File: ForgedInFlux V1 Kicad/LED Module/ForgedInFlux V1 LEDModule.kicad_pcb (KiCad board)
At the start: 2 copper layers, 59.6 x 99.6 mm, 0 parts

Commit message: Edited Schematic
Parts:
- added D1: SK6812, LED_SMD:LED_SK6812_PLCC4_5.0x5.0mm_P3.2mm, F.Cu at (49.1, 56.3)
- added D10: SK6812, LED_SMD:LED_SK6812_PLCC4_5.0x5.0mm_P3.2mm, F.Cu at (57.5, 76.2)
- added D11: SK6812, LED_SMD:LED_SK6812_PLCC4_5.0x5.0mm_P3.2mm, F.Cu at (57.5, 82.8)
- added D12: SK6812, LED_SMD:LED_SK6812_PLCC4_5.0x5.0mm_P3.2mm, F.Cu at (57.5, 89.4)
- added D13: SK6812, LED_SMD:LED_SK6812_PLCC4_5.0x5.0mm_P3.2mm, F.Cu at (66.0, 56.3)
- added D14: SK6812, LED_SMD:LED_SK6812_PLCC4_5.0x5.0mm_P3.2mm, F.Cu at (66.0, 62.9)
- added D15: SK6812, LED_SMD:LED_SK6812_PLCC4_5.0x5.0mm_P3.2mm, F.Cu at (66.0, 69.5)
- added D2: SK6812, LED_SMD:LED_SK6812_PLCC4_5.0x5.0mm_P3.2mm, F.Cu at (49.1, 62.9)
- added D3: SK6812, LED_SMD:LED_SK6812_PLCC4_5.0x5.0mm_P3.2mm, F.Cu at (49.1, 69.5)
- added D4: SK6812, LED_SMD:LED_SK6812_PLCC4_5.0x5.0mm_P3.2mm, F.Cu at (49.1, 76.2)
- added D5: SK6812, LED_SMD:LED_SK6812_PLCC4_5.0x5.0mm_P3.2mm, F.Cu at (49.1, 82.8)
- added D6: SK6812, LED_SMD:LED_SK6812_PLCC4_5.0x5.0mm_P3.2mm, F.Cu at (49.1, 89.4)
- added D7: SK6812, LED_SMD:LED_SK6812_PLCC4_5.0x5.0mm_P3.2mm, F.Cu at (57.5, 56.3)
- added D8: SK6812, LED_SMD:LED_SK6812_PLCC4_5.0x5.0mm_P3.2mm, F.Cu at (57.5, 62.9)
- added D9: SK6812, LED_SMD:LED_SK6812_PLCC4_5.0x5.0mm_P3.2mm, F.Cu at (57.5, 69.5)

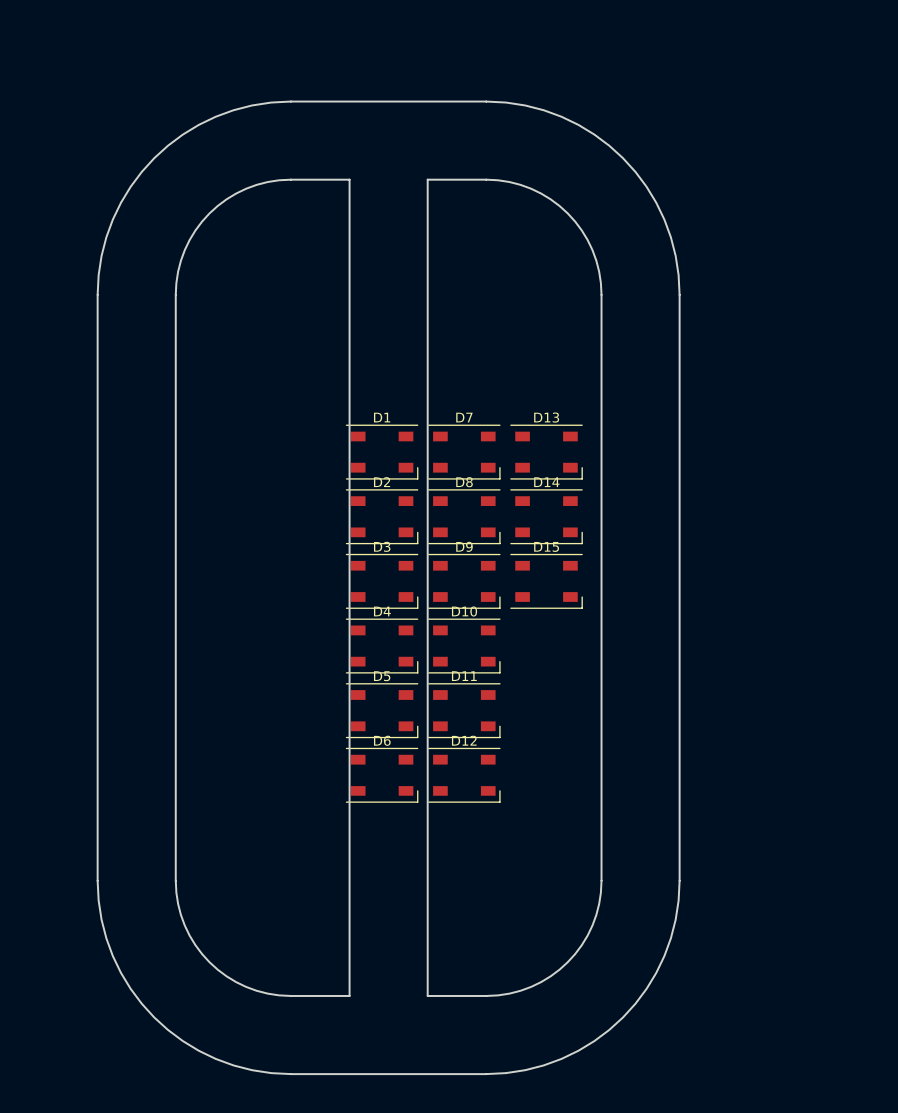
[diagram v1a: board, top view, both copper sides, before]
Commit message: Started Creating LEDModulePCB
- Edge cuts recompleted with adjusted dimensions
- Created custom footprints and schematic symbol for LED Pads
- Completed Schematic
- Layed out parts components onto a pcb and done rough wire tracing.
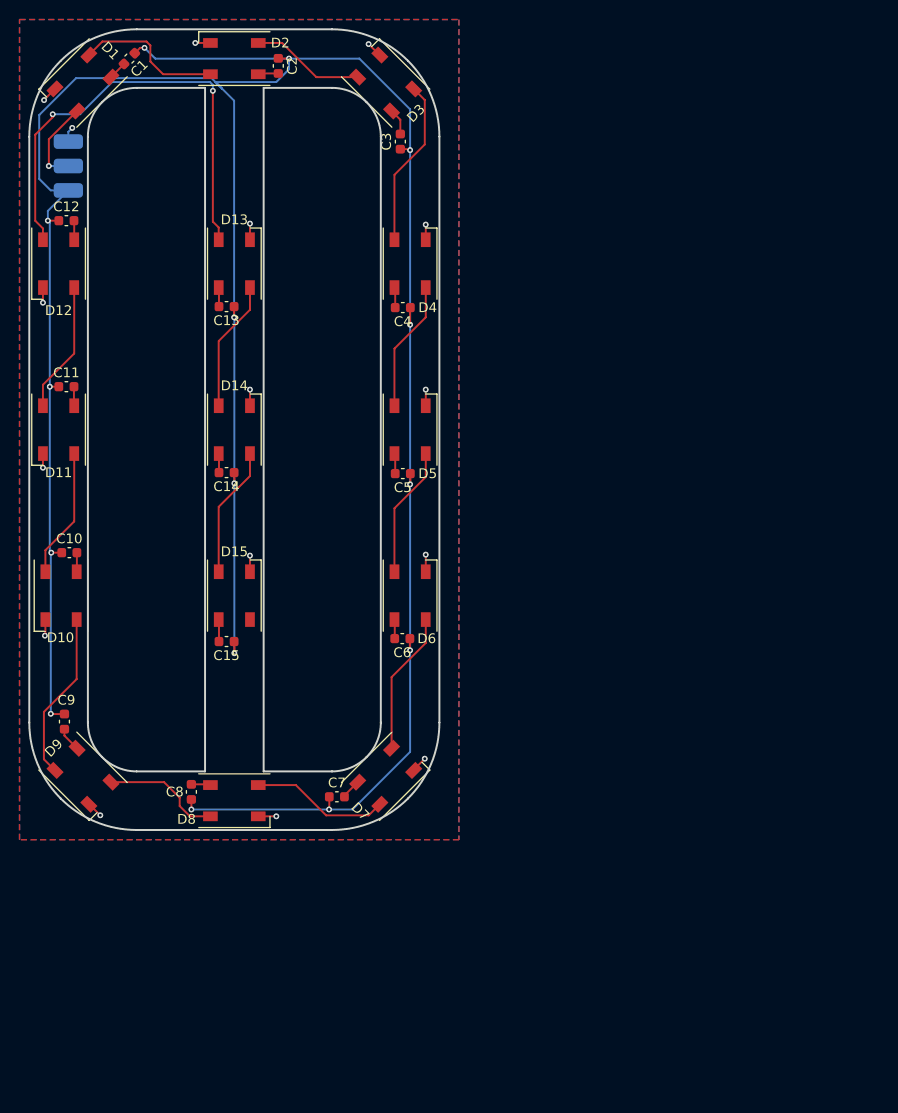
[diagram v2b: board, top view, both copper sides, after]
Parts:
- added C1: 0.1uF, Capacitor_SMD:C_0603_1608Metric, F.Cu at (23.2, 16.0)
- added C10: 0.1uF, Capacitor_SMD:C_0603_1608Metric, F.Cu at (17.1, 66.6)
- added C11: 0.1uF, Capacitor_SMD:C_0603_1608Metric, F.Cu at (16.8, 49.6)
- added C12: 0.1uF, Capacitor_SMD:C_0603_1608Metric, F.Cu at (16.8, 32.6)
- added C13: 0.1uF, Capacitor_SMD:C_0603_1608Metric, F.Cu at (33.2, 41.4)
- added C14: 0.1uF, Capacitor_SMD:C_0603_1608Metric, F.Cu at (33.2, 58.4)
- added C15: 0.1uF, Capacitor_SMD:C_0603_1608Metric, F.Cu at (33.2, 75.7)
- added C2: 0.1uF, Capacitor_SMD:C_0603_1608Metric, F.Cu at (38.5, 16.8)
- added C3: 0.1uF, Capacitor_SMD:C_0603_1608Metric, F.Cu at (51.0, 24.5)
- added C4: 0.1uF, Capacitor_SMD:C_0603_1608Metric, F.Cu at (51.2, 41.5)
- added C5: 0.1uF, Capacitor_SMD:C_0603_1608Metric, F.Cu at (51.2, 58.5)
- added C6: 0.1uF, Capacitor_SMD:C_0603_1608Metric, F.Cu at (51.2, 75.4)
- added C7: 0.1uF, Capacitor_SMD:C_0603_1608Metric, F.Cu at (44.5, 91.6)
- added C8: 0.1uF, Capacitor_SMD:C_0603_1608Metric, F.Cu at (29.6, 91.1)
- added C9: 0.1uF, Capacitor_SMD:C_0603_1608Metric, F.Cu at (16.6, 83.9)
- added LEDPads1: ~, LEDModuleLibrary:Led Pads, B.Cu at (17.0, 29.5)
- moved D12 66.9 mm to (16.0, 37.0), turned to -90 degrees
- moved D3 51.0 mm to (49.5, 18.5), turned to 135 degrees
- moved D11 50.5 mm to (16.0, 54.0), turned to -90 degrees
- moved D2 49.3 mm to (34.0, 16.0), turned to 180 degrees
- moved D1 48.7 mm to (18.5, 18.5), turned to -135 degrees
- moved D9 43.9 mm to (18.5, 89.5), turned to -45 degrees
- moved D10 41.6 mm to (16.2, 71.0), turned to -90 degrees
- moved D4 39.3 mm to (52.0, 37.0), turned to 90 degrees
- moved D8 37.4 mm to (34.0, 92.0)
- moved D13 37.3 mm to (34.0, 37.0), turned to 90 degrees
- moved D7 34.2 mm to (49.5, 89.5), turned to 45 degrees
- moved D14 33.2 mm to (34.0, 54.0), turned to 90 degrees
- moved D15 32.0 mm to (34.0, 71.0), turned to 90 degrees
- moved D5 28.9 mm to (52.0, 54.0), turned to 90 degrees
- moved D6 18.6 mm to (52.0, 71.0), turned to 90 degrees
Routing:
- net +5V: track 0.00 -> 292.0 mm, vias 0 -> 15
- net Net-(D12-DOUT): track 0.00 -> 47.9 mm, vias 0 -> 2
- net GND: track 0.00 -> 26.1 mm, vias 0 -> 16
- net Net-(D10-DIN): track 0.00 -> 17.3 mm
- net Net-(D3-DOUT): track 0.00 -> 17.2 mm
- net Net-(D1-DOUT): track 0.00 -> 15.4 mm
- net Net-(D6-DOUT): track 0.00 -> 14.6 mm
- net Net-(D7-DOUT): track 0.00 -> 14.2 mm
- net Net-(D14-DOUT): track 0.00 -> 13.5 mm
- net Net-(D5-DOUT): track 0.00 -> 13.4 mm
- net Net-(D4-DOUT): track 0.00 -> 13.4 mm
- net Net-(D13-DOUT): track 0.00 -> 13.4 mm
- net Net-(D11-DOUT): track 0.00 -> 13.4 mm
- net Net-(D10-DOUT): track 0.00 -> 13.3 mm
- net Net-(D8-DOUT): track 0.00 -> 12.1 mm
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- added copper zone on B.Cu, net GND
- added copper zone on F.Cu, net GND
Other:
- board size 59.6 x 99.6 mm -> 42 x 82 mm

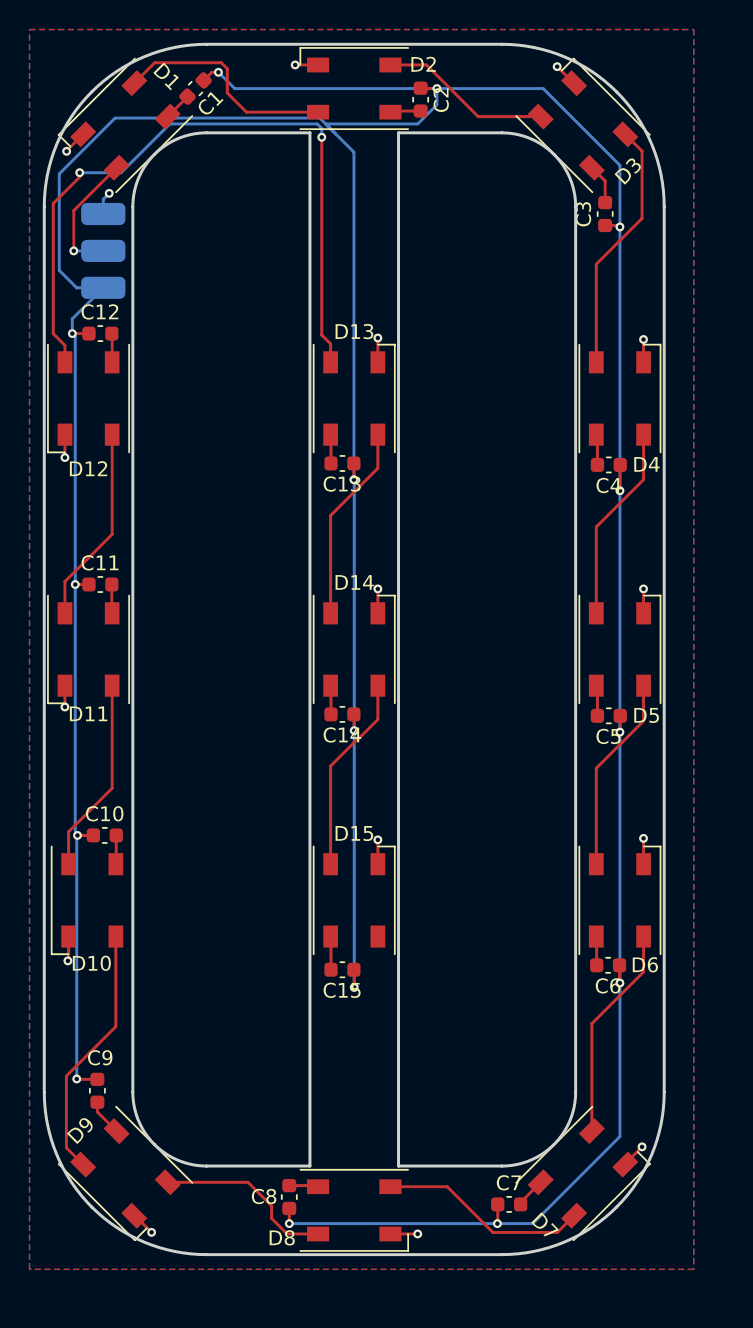
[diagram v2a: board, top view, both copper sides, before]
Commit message: Updates to schematic
- Changed Capacitor from Series to Parrallel
- Thickened PCB Traces
- Changed GND fill layers to 1 GND and 1 5V
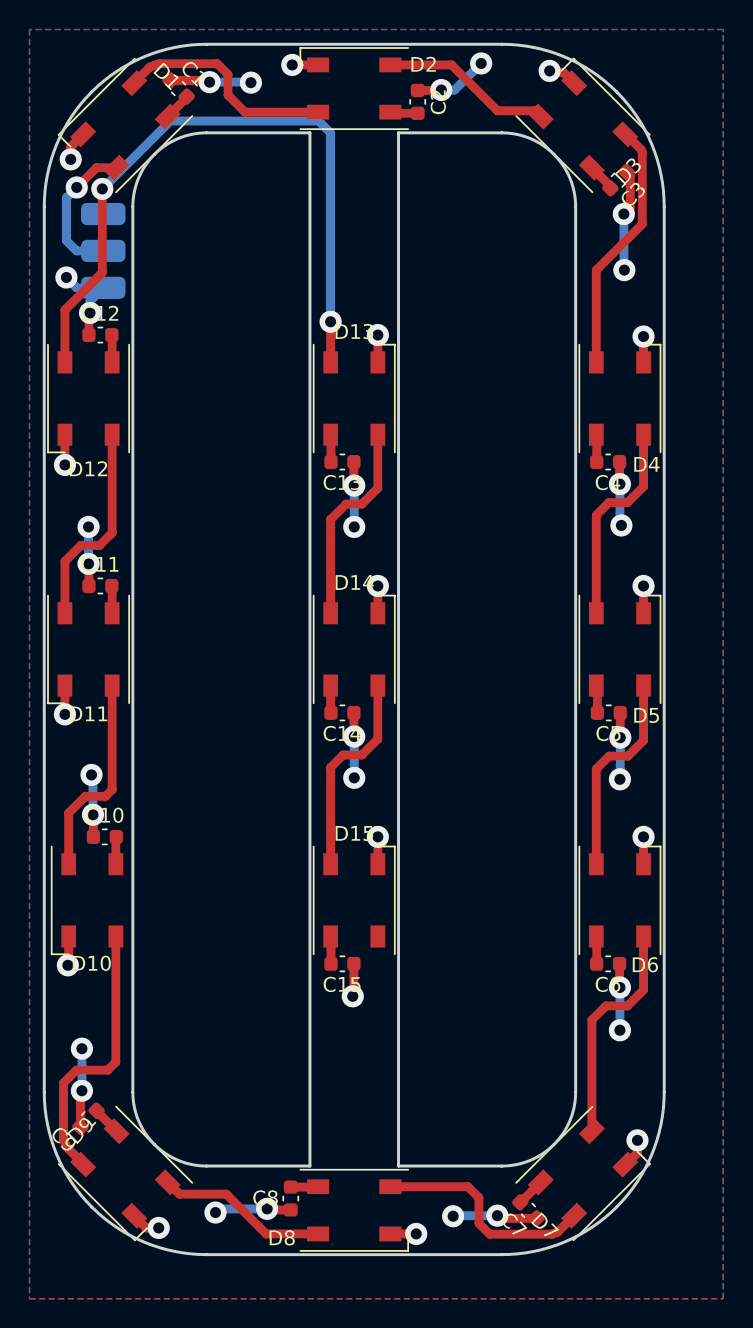
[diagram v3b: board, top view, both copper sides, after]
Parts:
- moved C3 2.47 mm to (51.9, 22.2), turned to -135 degrees
- moved C9 1.99 mm to (16.0, 85.8), turned to 45 degrees
- moved C7 1.36 mm to (45.8, 92.0), turned to 135 degrees
- moved C1 1.15 mm to (22.1, 16.0), turned to -45 degrees
- moved C15 0.40 mm to (33.2, 75.3)
- moved C2 0.25 mm to (38.3, 16.9)
- moved C4 0.21 mm to (51.2, 41.3)
- moved C5 0.20 mm to (51.2, 58.3)
- moved C8 0.14 mm to (29.7, 91.2)
- moved C10 0.10 mm to (17.1, 66.7)
- moved C6 0.10 mm to (51.2, 75.3)
- moved C11 0.10 mm to (16.8, 49.7)
- moved C12 0.10 mm to (16.8, 32.7)
- moved C13 0.10 mm to (33.2, 41.3)
- moved C14 0.10 mm to (33.2, 58.3)
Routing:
- net +5V: track 292.0 -> 72.9 mm, vias 15 -> 29
- net GND: track 26.1 -> 28.5 mm, vias 16 -> 15
- net Net-(D12-DOUT): track 47.9 -> 46.1 mm
- net Net-(D10-DIN): track 17.3 -> 18.7 mm
- net LEDData: track 8.84 -> 9.93 mm
- net Net-(D7-DOUT): track 14.2 -> 15.3 mm
- net Net-(D6-DOUT): track 14.6 -> 15.5 mm
- net Net-(D10-DOUT): track 13.3 -> 14.1 mm
- net Net-(D3-VDD): track 2.73 -> 1.94 mm
- net Net-(D5-DOUT): track 13.4 -> 14.2 mm
- net Net-(D4-DOUT): track 13.4 -> 14.2 mm
- net Net-(D11-DOUT): track 13.4 -> 14.2 mm
- net Net-(D14-DOUT): track 13.5 -> 14.2 mm
- net Net-(D13-DOUT): track 13.4 -> 14.1 mm
- net Net-(D9-VDD): track 2.50 -> 1.94 mm
- added copper zone on F.Cu, net +5V
- removed copper zone on F.Cu, net GND

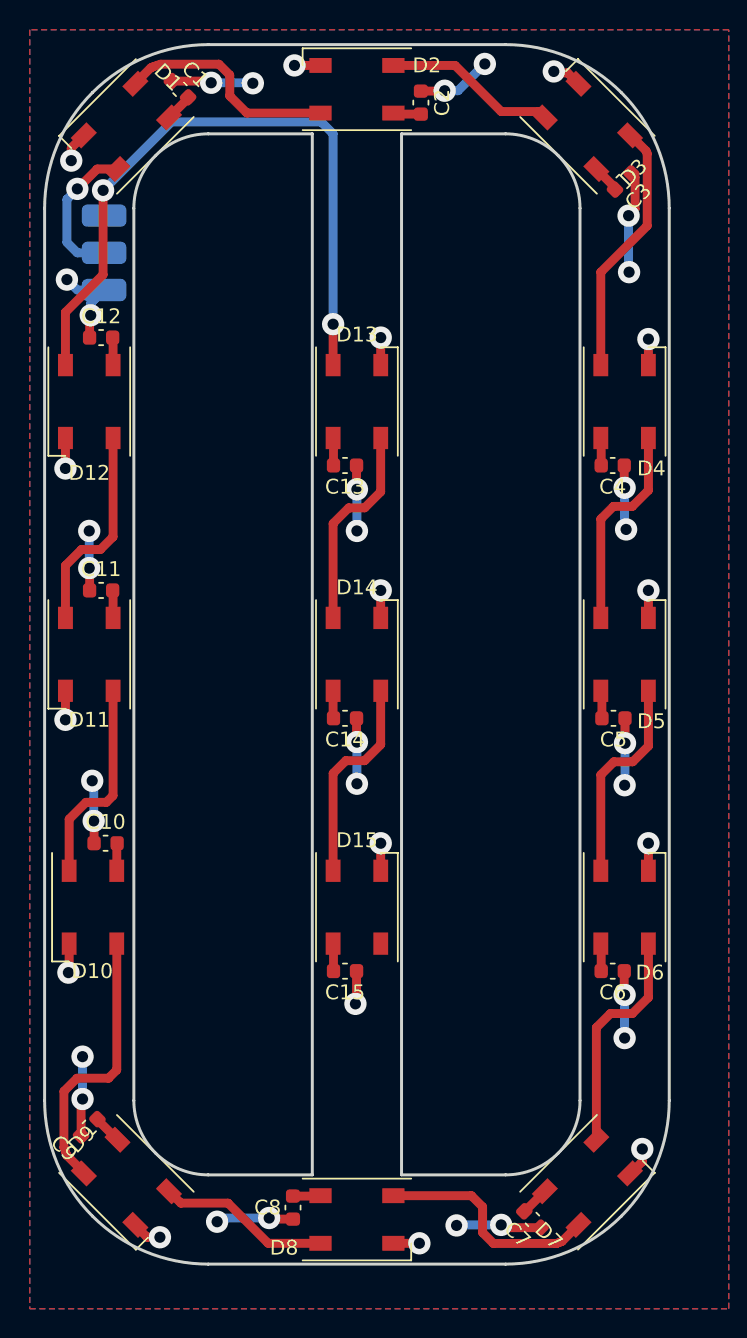
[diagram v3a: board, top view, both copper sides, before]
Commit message: Continued Development of Design
LEDModule Schematic and PCB need to be reworked for accommodation of hand soldered parts
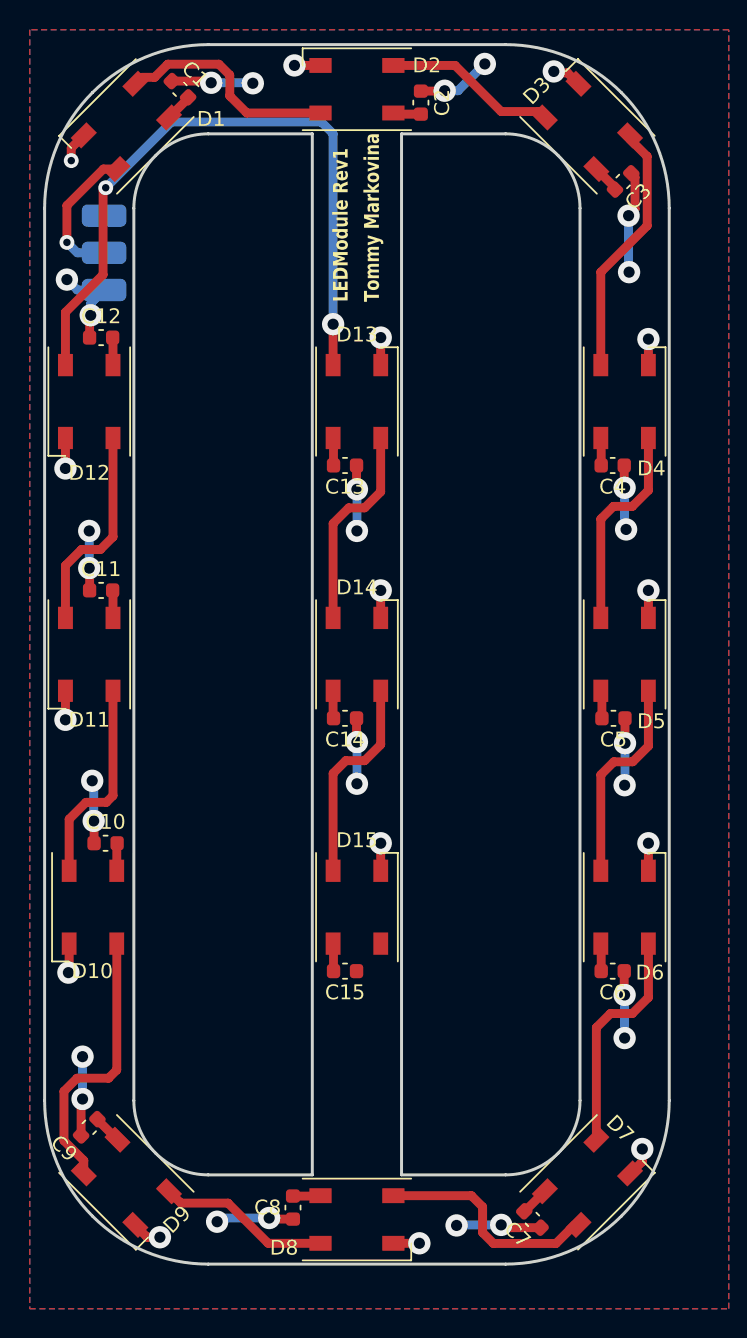
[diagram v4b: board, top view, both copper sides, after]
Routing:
- net +5V: track 72.9 -> 70.7 mm, vias 29 -> 28
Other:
- board text added: "LEDModule Rev1"
- board text added: "Tommy Markovina"
